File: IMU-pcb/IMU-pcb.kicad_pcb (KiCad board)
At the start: 2 copper layers, 12 parts, among them J1 Conn_01x05_Female, U1 4056Board, U2 WeMos_D1_mini, U3 4754

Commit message: formalized schematic, symbols, and footprints
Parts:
- added J1: Status Rails, bryx-comp-lib:fivePinConn, F.Cu at (193.0, 63.5)
- J2: renamed from Battery1; value Conn_01x02_Female -> Battery
- J3: renamed from J1; value Conn_01x05_Female -> AUX Sensor
- U3: value 4754 -> IMU Sensor
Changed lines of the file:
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@@
   (net 1 "B+")
   (net 2 "B-")
-  (net 3 "Net-(R1-Pad2)")
-  (net 4 "Net-(R3-Pad1)")
+  (net 3 "Net-(D1-Pad1)")
+  (net 4 "Net-(D1-Pad2)")
   (net 5 "5V")
-  (net 6 "Net-(U1-Pad5)")
-  (net 7 "Net-(U1-Pad1)")
+  (net 6 "Net-(D2-Pad2)")
+  (net 7 "Net-(D3-Pad2)")
   (net 8 "3V3")
   (net 9 "Switch_GND")
@@
   (net 12 "INT_PIN2")
   (net 13 "Net-(R2-Pad2)")
-  (net 14 "Net-(U2-Pad7)")
-  (net 15 "Net-(U1-Pad4)")
+  (net 14 "Net-(R3-Pad2)")
+  (net 15 "Net-(S1-Pad1)")
   (net 16 "unconnected-(U1-Pad6)")
   (net 17 "unconnected-(U3-PadJP1_2)")
@@
     (property "Sheetname" "")
     (attr through_hole)
-    (fp_text reference "Battery1" (at 1.5 -2.45) (layer "F.SilkS")
-      (effects (font (size 1 1) (thickness 0.15)))
-    )
-    (fp_text value "Conn_01x02_Female" (at 1 7.25) (layer "F.Fab")
+    (fp_text reference "J2" (at 1.5 -2.45) (layer "F.SilkS")
+      (effects (font (size 1 1) (thickness 0.15)))
+    )
+    (fp_text value "Battery" (at 1 7.25) (layer "F.Fab")
       (effects (font (size 1 1) (thickness 0.15)))
     )
@@
     (fp_line (start -1 -5) (end 1 -5) (layer "F.SilkS") (width 0.12))
     (pad "1" thru_hole circle (at 0 -3.5) (size 2 2) (drill 0.762) (layers *.Cu *.Mask)
-      (net 4 "Net-(R3-Pad1)") (pintype "passive"))
+      (net 4 "Net-(D1-Pad2)") (pintype "passive"))
     (pad "2" thru_hole circle (at 0 3.5) (size 2 2) (drill 0.762) (layers *.Cu *.Mask)
-      (net 14 "Net-(U2-Pad7)") (pintype "passive"))
+      (net 14 "Net-(R3-Pad2)") (pintype "passive"))
   )
   (footprint "SlimeVRMotherBoard:180KΩ" (layer "F.Cu")
@@
       (net 25 "unconnected-(U2-Pad6)") (pinfunction "D7") (pintype "bidirectional+no_connect"))
     (pad "7" thru_hole circle locked (at -6.35 -11.43) (size 1.8 1.8) (drill 1.016) (layers *.Cu *.Mask)
-      (net 14 "Net-(U2-Pad7)") (pinfunction "D8") (pintype "bidirectional"))
+      (net 14 "Net-(R3-Pad2)") (pinfunction "D8") (pintype "bidirectional"))
     (pad "8" thru_hole circle locked (at -8.89 -11.43) (size 1.8 1.8) (drill 1.016) (layers *.Cu *.Mask)
       (net 8 "3V3") (pinfunction "3.3V") (pintype "power_out"))
@@
       (net 9 "Switch_GND") (pintype "passive"))
     (pad "2" thru_hole circle (at 0 3.5) (size 2 2) (drill 0.762) (layers *.Cu *.Mask)
-      (net 3 "Net-(R1-Pad2)") (pintype "passive"))
+      (net 3 "Net-(D1-Pad1)") (pintype "passive"))
   )
   (footprint "BNO085:BNO085" (layer "F.Cu")
@@
       (effects (font (size 1 1) (thickness 0.15)))
     )
-    (fp_text value "4754" (at -5.965 13.315) (layer "F.Fab")
+    (fp_text value "IMU Sensor" (at -5.965 13.315) (layer "F.Fab")
       (effects (font (size 1 1) (thickness 0.15)))
     )
@@
     (pad "P4" thru_hole circle locked (at 10.16 8.89) (size 3.2 3.2) (drill 2.5) (layers *.Cu *.Mask))
   )
+  (footprint "bryx-comp-lib:fivePinConn" (layer "F.Cu")
+    (at 193.04 63.5)
+    (property "Sheetfile" "IMU-pcb.kicad_sch")
+    (property "Sheetname" "")
+    (attr through_hole)
+    (fp_text reference "J1" (at 0 5.08) (layer "F.SilkS")
+      (effects (font (size 1 1) (thickness 0.15)))
+    )
+    (fp_text value "Status Rails" (at 0 3.81) (layer "F.Fab")
+      (effects (font (size 1 1) (thickness 0.15)))
+    )
+    (pad "1" thru_hole circle locked (at -5.08 0) (size 1.524 1.524) (drill 0.762) (layers *.Cu *.Mask)
+      (net 5 "5V") (pinfunction "Pin_1") (pintype "passive"))
+    (pad "2" thru_hole circle locked (at -2.54 0) (size 1.524 1.524) (drill 0.762) (layers *.Cu *.Mask)
+      (net 8 "3V3") (pinfunction "Pin_2") (pintype "passive"))
+    (pad "3" thru_hole circle locked (at 0 0) (size 1.524 1.524) (drill 0.762) (layers *.Cu *.Mask)
+      (net 9 "Switch_GND") (pinfunction "Pin_3") (pintype "passive"))
+    (pad "4" thru_hole circle locked (at 2.54 0) (size 1.524 1.524) (drill 0.762) (layers *.Cu *.Mask)
+      (net 1 "B+") (pinfunction "Pin_4") (pintype "passive"))
+    (pad "5" thru_hole circle locked (at 5.08 0) (size 1.524 1.524) (drill 0.762) (layers *.Cu *.Mask)
+      (net 2 "B-") (pinfunction "Pin_5") (pintype "passive"))
+  )
   (footprint "SlimeVRMotherBoard:Wowoone_Slide_Switch_5mm" (layer "F.Cu")
     (at 120.37 84.67)
@@
     (fp_line (start 6.4 -3.35) (end -6.4 -3.35) (layer "F.SilkS") (width 0.2))
     (pad "1" thru_hole circle locked (at -4.8 0) (size 2.5 2.5) (drill 1.5) (layers *.Cu *.Mask)
-      (net 15 "Net-(U1-Pad4)") (pinfunction "T1") (pintype "input"))
+      (net 15 "Net-(S1-Pad1)") (pinfunction "T1") (pintype "input"))
     (pad "2" thru_hole circle locked (at 0 0) (size 2.5 2.5) (drill 1.5) (layers *.Cu *.Mask)
       (net 9 "Switch_GND") (pinfunction "T2") (pintype "output"))
@@
     (property "Sheetname" "")
     (attr through_hole)
-    (fp_text reference "J1" (at 5 -3.5) (layer "F.SilkS")
-      (effects (font (size 1 1) (thickness 0.15)))
-    )
-    (fp_text value "Conn_01x05_Female" (at 5 10.3) (layer "F.Fab")
+    (fp_text reference "J3" (at 5 -3.5) (layer "F.SilkS")
+      (effects (font (size 1 1) (thickness 0.15)))
+    )
+    (fp_text value "AUX Sensor" (at 5 10.3) (layer "F.Fab")
       (effects (font (size 1 1) (thickness 0.15)))
     )
@@
       (net 5 "5V") (pinfunction "K") (pintype "passive"))
     (pad "2" thru_hole oval (at 10.16 0) (size 2.2 2.2) (drill 1.1) (layers *.Cu *.Mask)
-      (net 7 "Net-(U1-Pad1)") (pinfunction "A") (pintype "passive"))
+      (net 7 "Net-(D3-Pad2)") (pinfunction "A") (pintype "passive"))
     (model "${KICAD6_3DMODEL_DIR}/Diode_THT.3dshapes/D_DO-41_SOD81_P10.16mm_Horizontal.wrl"
       (offset (xyz 0 0 0))
@@
     (fp_circle (center 1.27 0) (end 3.77 0) (layer "F.Fab") (width 0.1) (fill none))
     (pad "1" thru_hole rect (at 0 0) (size 1.8 1.8) (drill 0.9) (layers *.Cu *.Mask)
-      (net 3 "Net-(R1-Pad2)") (pinfunction "K") (pintype "passive"))
+      (net 3 "Net-(D1-Pad1)") (pinfunction "K") (pintype "passive"))
     (pad "2" thru_hole circle (at 2.54 0) (size 1.8 1.8) (drill 0.9) (layers *.Cu *.Mask)
-      (net 4 "Net-(R3-Pad1)") (pinfunction "A") (pintype "passive"))
+      (net 4 "Net-(D1-Pad2)") (pinfunction "A") (pintype "passive"))
     (model "${KICAD6_3DMODEL_DIR}/LED_THT.3dshapes/LED_D5.0mm.wrl"
       (offset (xyz 0 0 0))
@@
     (fp_line (start 8.5 -14) (end 8.5 14) (layer "F.SilkS") (width 0.12))
     (pad "1" thru_hole circle locked (at -7 -10.5) (size 2 2) (drill 1.2) (layers *.Cu *.Mask)
-      (net 7 "Net-(U1-Pad1)") (pinfunction "Out+") (pintype "output"))
+      (net 7 "Net-(D3-Pad2)") (pinfunction "Out+") (pintype "output"))
     (pad "2" thru_hole circle locked (at -4 -10.5) (size 2 2) (drill 1.2) (layers *.Cu *.Mask)
       (net 1 "B+") (pinfunction "Battery+") (pintype "input"))
@@
       (net 2 "B-") (pinfunction "Battery-") (pintype "input"))
     (pad "4" thru_hole circle locked (at 7 -10.5) (size 2 2) (drill 1.2) (layers *.Cu *.Mask)
-      (net 15 "Net-(U1-Pad4)") (pinfunction "Out-") (pintype "output"))
+      (net 15 "Net-(S1-Pad1)") (pinfunction "Out-") (pintype "output"))
     (pad "5" thru_hole circle locked (at -7 12) (size 2 2) (drill 1.2) (layers *.Cu *.Mask)
-      (net 6 "Net-(U1-Pad5)") (pinfunction "RB+") (pintype "output"))
+      (net 6 "Net-(D2-Pad2)") (pinfunction "RB+") (pintype "output"))
     (pad "6" thru_hole circle locked (at 7 12) (size 2 2) (drill 1.2) (layers *.Cu *.Mask)
       (net 16 "unconnected-(U1-Pad6)") (pinfunction "RB-") (pintype "no_connect"))
@@
       (net 5 "5V") (pinfunction "K") (pintype "passive"))
     (pad "2" thru_hole oval (at 10.16 0) (size 2.2 2.2) (drill 1.1) (layers *.Cu *.Mask)
-      (net 6 "Net-(U1-Pad5)") (pinfunction "A") (pintype "passive"))
+      (net 6 "Net-(D2-Pad2)") (pinfunction "A") (pintype "passive"))
     (model "${KICAD6_3DMODEL_DIR}/Diode_THT.3dshapes/D_DO-41_SOD81_P10.16mm_Horizontal.wrl"
       (offset (xyz 0 0 0))

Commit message: Starting pcb layout
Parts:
- moved J1 107.7 mm to (90.2, 95.2)
- moved U2 83.2 mm to (96.5, 114.3), turned to 90 degrees
- moved R2 67.8 mm to (102.9, 95.2), turned to -90 degrees
- moved J2 65.5 mm to (114.0, 98.6)
- moved D2 62.0 mm to (120.7, 104.1)
- moved D3 61.4 mm to (120.7, 99.1)
- moved U3 61.1 mm to (123.2, 119.4), turned to 90 degrees
- moved U1 58.0 mm to (144.8, 118.1)
- moved D1 56.4 mm to (137.9, 96.5), turned to 180 degrees
- moved J3 44.0 mm to (156.6, 116.8), turned to 90 degrees
- moved R1 38.5 mm to (151.1, 101.6), turned to -90 degrees
- moved S1 29.4 mm to (147.3, 96.5)
- moved R3 23.9 mm to (138.4, 101.6), turned to -90 degrees

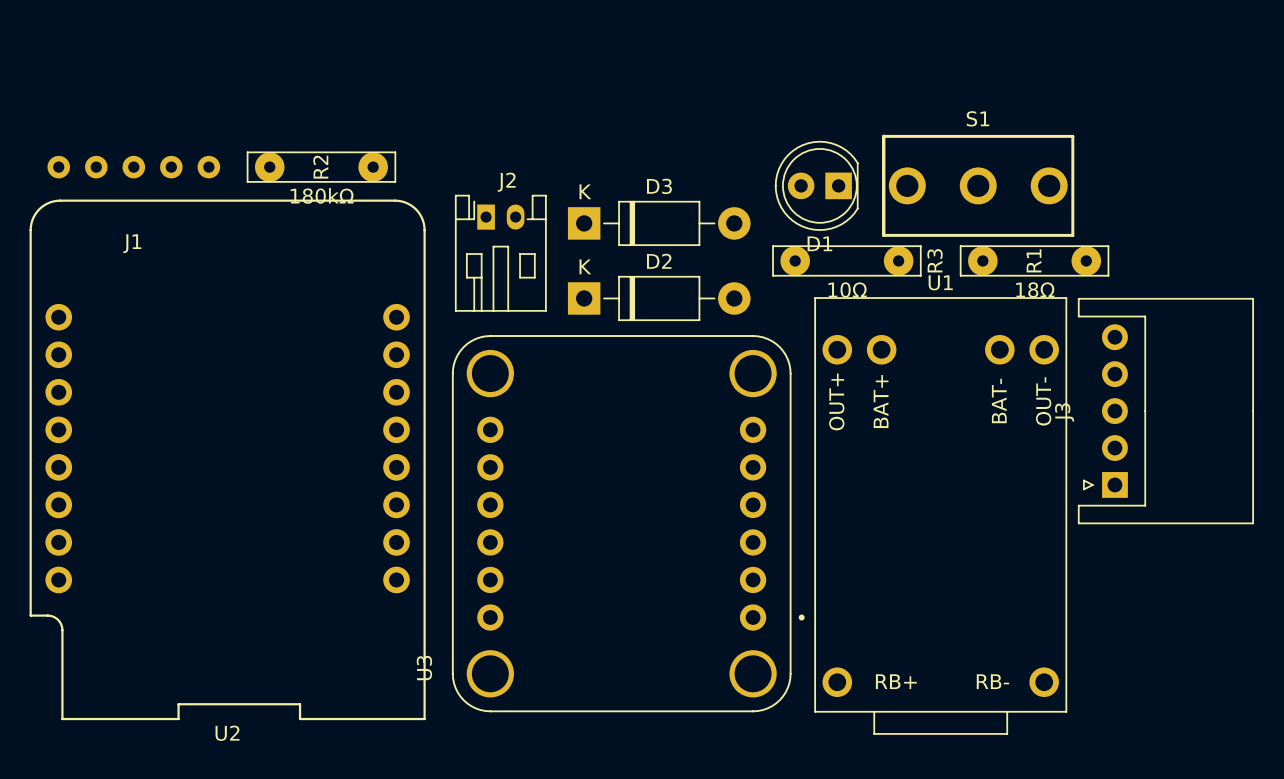
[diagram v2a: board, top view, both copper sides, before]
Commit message: Adjusting pcb layout to fit for the dimensions
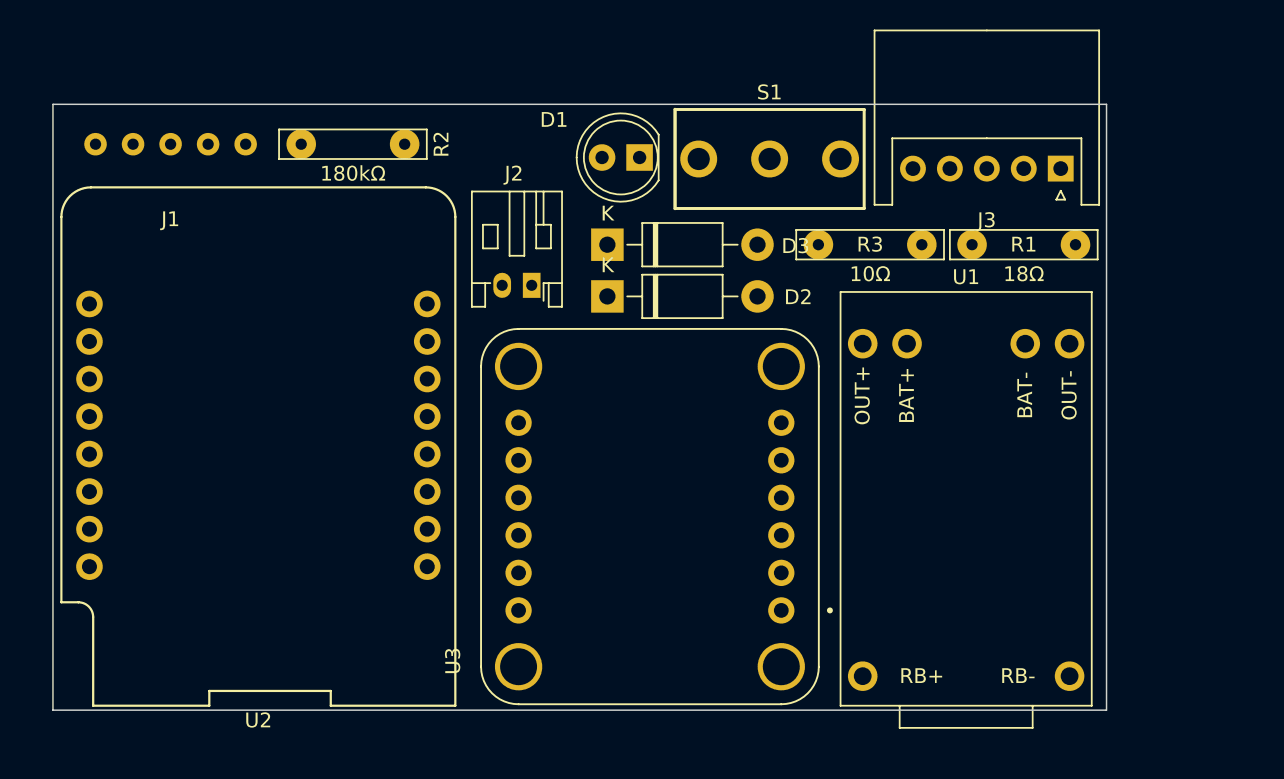
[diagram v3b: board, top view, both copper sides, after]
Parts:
- D2, D3: footprint Diode_THT:D_DO-41_SOD81_P10.16mm_Horizontal -> PLANETS:D_DO-41_SOD81_P10.16mm_Horizontal
- J1: footprint bryx-comp-lib:fivePinConn -> PLANETS:fivePinConn
- J2: footprint Connectors_JST:JST_PH_S2B-PH-K_02x2.00mm_Angled -> PLANETS:JST_PH_S2B-PH-K_02x2.00mm_Angled
- J3: footprint Connectors_JST:JST_XH_S05B-XH-A_05x2.50mm_Angled -> PLANETS:JST_XH_S05B-XH-A_05x2.50mm_Angled
- R1: footprint SlimeVRMotherBoard:18Ω -> PLANETS:18Ω
- R2: footprint SlimeVRMotherBoard:180KΩ -> PLANETS:180KΩ
- R3: footprint SlimeVRMotherBoard:10Ω -> PLANETS:10Ω
- S1: footprint SlimeVRMotherBoard:Wowoone_Slide_Switch_5mm -> PLANETS:Wowoone_Slide_Switch_5mm
- U1: footprint SlimeVRMotherBoard:4056Board -> PLANETS:4056Board
- U2: footprint wemos-d1-mini:wemos-d1-mini-with-pin-header-and-connector -> PLANETS:wemos-d1-mini-with-pin-header-and-connector
- U3: footprint BNO085:BNO085 -> PLANETS:BNO085
- moved J3 21.7 mm to (152.9, 95.3), turned to 180 degrees
- moved S1 14.2 mm to (133.2, 94.7)
- moved D1 13.6 mm to (124.4, 94.6)
- moved J2 5.56 mm to (117.1, 103.2), turned to 180 degrees
- moved J1 2.93 mm to (92.7, 93.7)
- moved R2 2.63 mm to (105.0, 93.7)
- moved U2 2.27 mm to (98.6, 113.4)
- moved D3 2.13 mm to (122.2, 100.5)
- moved U3 1.97 mm to (125.1, 118.9)
- moved R3 1.92 mm to (140.0, 100.5)
- moved U1 1.77 mm to (146.5, 117.7)
- moved D2 1.58 mm to (122.2, 104.0)
- moved R1 1.32 mm to (150.4, 100.5)
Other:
- board outline added: 71.3 x 41 mm

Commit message: working on desktop
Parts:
- D1: footprint LED_THT:LED_D5.0mm -> PLANETS:LED_D5.0mm
- D2, D3: footprint PLANETS:D_DO-41_SOD81_P10.16mm_Horizontal -> Diode_THT:D_DO-41_SOD81_P10.16mm_Horizontal
- moved J3 22.3 mm to (159.1, 116.8), turned to 90 degrees
- moved S1 15.9 mm to (149.1, 94.8)
- moved D1 15.7 mm to (140.1, 94.8)
- moved J2 0.57 mm to (117.5, 103.6)
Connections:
- S1 pad 1: Net-(S1-Pad1) -> Switch_GND
- S1 pad 2: Switch_GND -> Net-(S1-Pad2)
- U1 pad 4: Net-(S1-Pad1) -> Net-(S1-Pad2)

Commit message: Finished PCB layout and gerbers
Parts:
- moved U2 33.6 mm to (123.9, 91.2)
- moved D1 33.5 mm to (165.4, 72.8)
- moved D2 33.5 mm to (147.5, 82.0)
- moved D3 33.5 mm to (147.5, 78.5)
- moved R2 33.5 mm to (130.3, 71.7)
- moved R3 33.5 mm to (165.3, 78.5)
- moved J1 33.5 mm to (118.0, 71.7)
- moved J2 33.5 mm to (142.8, 81.6)
- moved R1 33.5 mm to (175.7, 78.5)
- moved S1 33.5 mm to (174.3, 72.8)
- moved U1 33.3 mm to (171.5, 95.7)
- moved U3 33.3 mm to (150.0, 96.8)
- moved J3 33.2 mm to (183.8, 94.5)
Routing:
- net Switch_GND: track 0.00 -> 143.7 mm
- net 5V: track 0.00 -> 84.0 mm
- net Net-(R3-Pad2): track 0.00 -> 71.4 mm
- net B-: track 0.00 -> 59.3 mm
- net B+: track 0.00 -> 58.8 mm
- net INT_PIN1: track 0.00 -> 54.9 mm
- net SCL: track 0.00 -> 54.3 mm
- net SDA: track 0.00 -> 52.9 mm
- net 3V3: track 0.00 -> 31.8 mm
- net Net-(D2-Pad2): track 0.00 -> 28.5 mm
- net Net-(R2-Pad2): track 0.00 -> 23.7 mm
- net Net-(S1-Pad2): track 0.00 -> 14.1 mm
- net Net-(D3-Pad2): track 0.00 -> 9.60 mm
- net Net-(R1-Pad2): track 0.00 -> 9.21 mm
- net Net-(R3-Pad1): track 0.00 -> 9.16 mm
- added copper zone on B.Cu, net 3V3
- added copper zone on F.Cu, net INT_PIN2
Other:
- board size 71.3 x 41 mm -> 76.8 x 41 mm
- board text added: "PLANETS v1.0"

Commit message: Finished v1.1 layout
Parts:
- removed the D1 at (165.4, 72.8)
- removed the R1 at (175.7, 78.5)
- removed R3: 10, PLANETS:10Ω
- added ?: , PLANETS:pcb_patch, B.Cu at (123.8, 96.7)
- added D3: LED_RGBK, LED_THT:LED_D5.0mm-4_RGB, F.Cu at (161.1, 78.0)
- added R2: 150, PLANETS:150Ω, F.Cu at (151.1, 74.9)
- moved S1 6.68 mm to (173.8, 79.5)
- moved U1 0.45 mm to (171.5, 95.2)
- turned U3 to -90 degrees
- renumbered D2 to D1, D3 to D2, R2 to R1
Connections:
- net 3V3 renamed +3.3V
- D1 pad 1: 5V -> Net-(D1-Pad1)
- D2 pad 1: 5V -> Net-(D1-Pad1)
- J1 pad 1: 5V -> +5V
- J1 pad 3: Switch_GND -> GND
- J3 pad 2: Switch_GND -> GND
- J3 pad 3: SCL -> SDA
- J3 pad 4: SDA -> SCL
- S1 pad 1: Switch_GND -> +5V
- S1 pad 2: Net-(S1-Pad2) -> Net-(D1-Pad1)
- U1 pad 4: Net-(S1-Pad2) -> GND
- U2 pad 10: Switch_GND -> GND
- U2 pad 3: unconnected-(U2-Pad3) -> INT_PIN2
- U2 pad 5: INT_PIN2 -> D6
- U2 pad 6: unconnected-(U2-Pad6) -> D7
- U2 pad 7: Net-(R3-Pad2) -> D8
- U2 pad 9: 5V -> +5V
- U3 pad JP1_3: Switch_GND -> GND
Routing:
- net Switch_GND: track 143.7 -> 0.00 mm
- net +5V: track 0.00 -> 120.4 mm
- net 5V: track 84.0 -> 0.00 mm
- net INT_PIN2: track 0.00 -> 83.7 mm
- net Net-(R3-Pad2): track 71.4 -> 0.00 mm
- net D8: track 0.00 -> 61.0 mm
- net D7: track 0.00 -> 58.7 mm
- net D6: track 0.00 -> 42.4 mm
- net Net-(D1-Pad1): track 0.00 -> 34.4 mm
- net +3.3V: track 31.8 -> 0.00 mm
- net GND: track 0.00 -> 24.6 mm, vias 0 -> 2
- net SDA: track 52.9 -> 67.9 mm
- net Net-(S1-Pad2): track 14.1 -> 0.00 mm
- net INT_PIN1: track 54.9 -> 43.3 mm
- net SCL: track 54.3 -> 65.7 mm
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- added copper zone on F.Cu, net +3.3V
- added copper zone on B.Cu, net GND
- removed copper zone on B.Cu, net +3.3V
- removed copper zone on F.Cu, net INT_PIN2
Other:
- outline, holes or cut-outs redrawn
- board text added: "Angela Hudak Corey Sheridan"
- board text added: "PLANET v1.1"
- board text removed: "PLANETS v1.0"
